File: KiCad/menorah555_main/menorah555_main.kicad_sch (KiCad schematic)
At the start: 100 parts, among them J1 USB_B_Micro, J2 Jack5.5x2.1, J3 Plug5.5x2.1, Q1 MMBT3904, Q10 MJD31, Q2 MMBT3904, Q3 MMBT3904, Q4 MMBT3904, Q5 MMBT3904, Q6 MMBT3904, Q7 MMBT3904, Q8 MMBT3904, Q9 MMBT3904, SW1 SW_Reed, SW2 SW_Reed, SW3 SW_Reed, SW4 SW_Reed, SW5 SW_Reed, SW6 SW_Reed, SW7 SW_Reed, SW8 SW_Reed, SW9 SW_DPDT, U1 TLC555, U2 TLC555, U3 TLC555, U4 TLC555, U5 TLC555, U6 TLC555, U7 TLC555, U8 TLC555, U9 TLC555

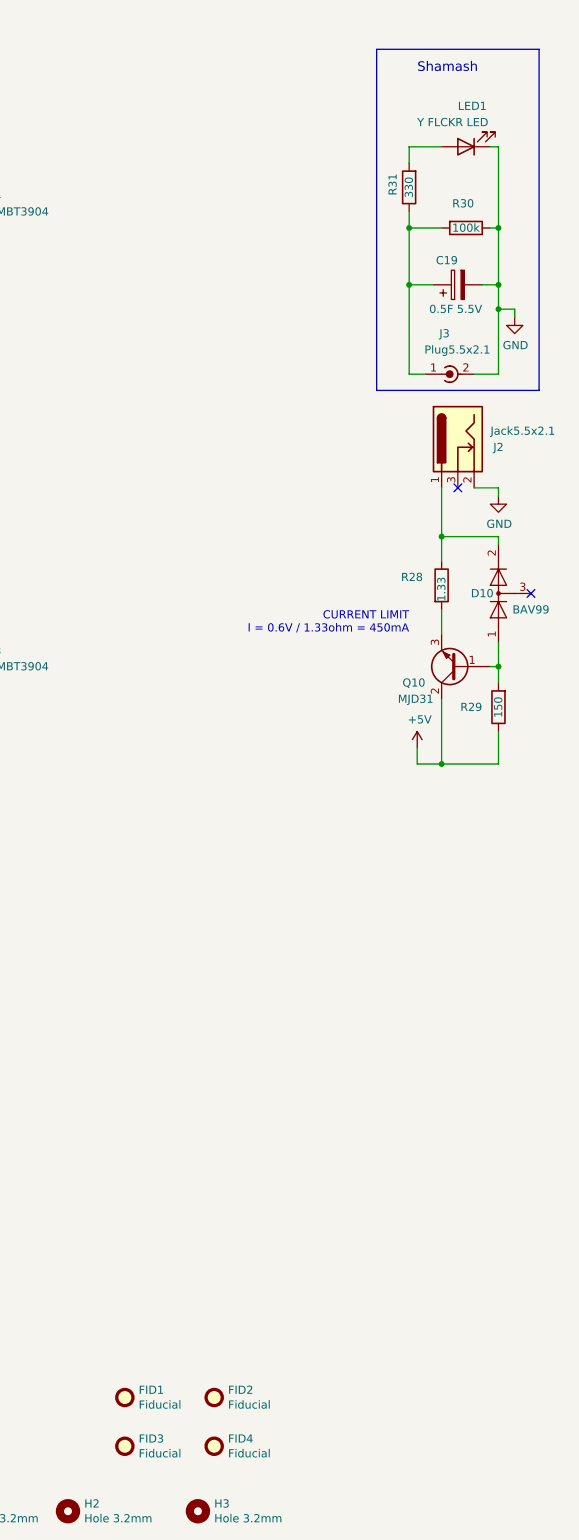
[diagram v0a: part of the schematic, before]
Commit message: Split PCB into separate main and shamash boards
Previously, the main and shamash PCBs were combined into one file.
Now they are separate PCBs so that they don't need to be cut apart and
smoothed.
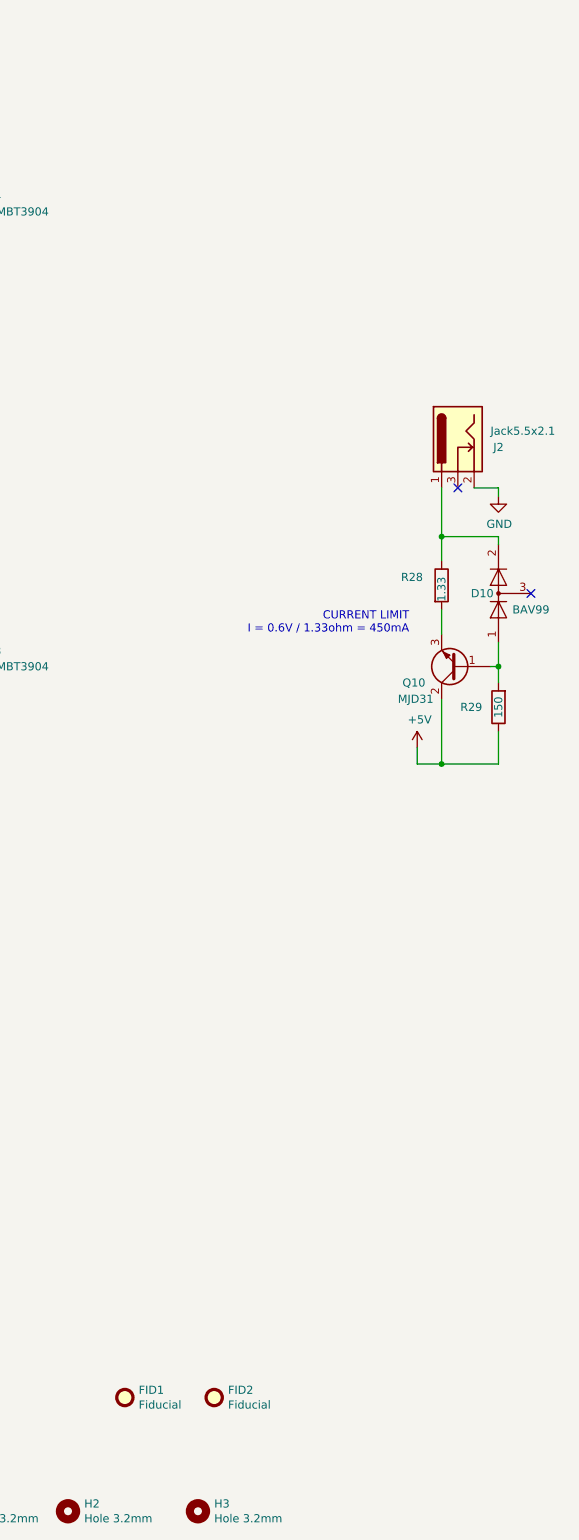
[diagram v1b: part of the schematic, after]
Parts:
- removed C19: 0.5F 5.5V, 0_my_footprints:CP_Supercap_DGH504Q5R5_Horizontal, symbol Device:CP
- removed FID3, FID4: Fiducial, Fiducial:Fiducial_1mm_Mask2mm, symbol Mechanical:Fiducial
- removed J3: Plug5.5x2.1, 0_my_footprints:KobiConn_173-5521TIP-EX_power_plug, symbol Connector:Conn_Coaxial_Power
- removed LED1: Y FLCKR LED, 0_my_footprints:LED_D5.0mm_Horizontal_SMT_O3.81mm_Z3.0mm, symbol Device:LED
- removed R30: 100k, Resistor_SMD:R_0805_2012Metric, symbol Device:R
- removed R31: 330, Resistor_SMD:R_0805_2012Metric, symbol Device:R
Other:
- note removed: "Shamash"
- title: Menorah555 -> Menorah555 Main

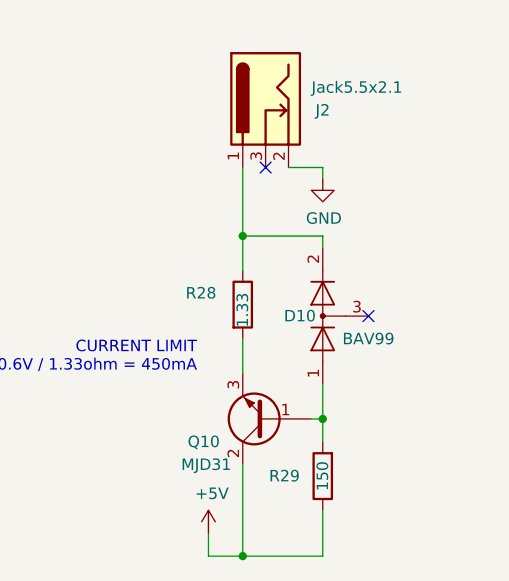
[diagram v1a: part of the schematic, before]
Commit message: Fixed long turn-off time
Previously on the rev A PCB (PCB2002A), when power was turned off, the
shamash would take a very long time (> 20 minutes) to fully turn off.
Now a new diode, D11, has been added to drain the supercap when power is
turned off with the switch.
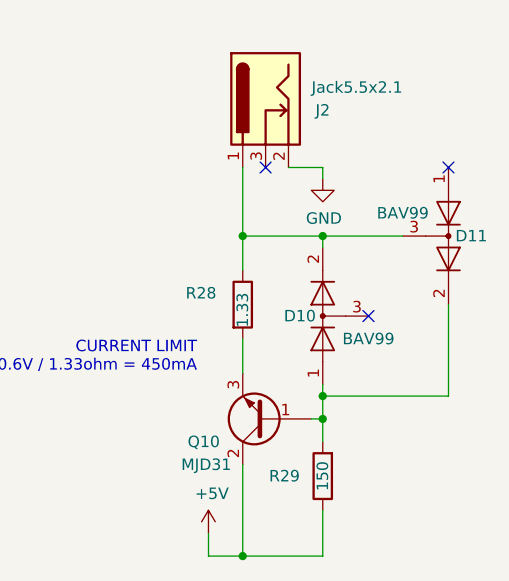
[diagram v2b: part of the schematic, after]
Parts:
- added D11: BAV99, Package_TO_SOT_SMD:SOT-23, symbol Diode:BAV99
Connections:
- net at D10.2 (A), J2.1, R28.1: now also D11.3 (K)
- net at D10.1 (K), Q10.1 (B), R29.2: now also D11.2 (A)
- no-connect marks 15 -> 16
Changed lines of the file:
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@@
   (junction (at 154.94 184.15) (diameter 0) (color 0 0 0 0)
   )
+  (junction (at 342.9 107.95) (diameter 0) (color 0 0 0 0)
+  )
   (junction (at 82.55 207.01) (diameter 0) (color 0 0 0 0)
   )
+  (junction (at 342.9 125.73) (diameter 0) (color 0 0 0 0)
+  )
   (junction (at 191.77 119.38) (diameter 0) (color 0 0 0 0)
   )
@@
   (no_connect (at 135.89 69.85))
   (no_connect (at 190.5 140.97))
+  (no_connect (at 356.87 100.33))
   (no_connect (at 246.38 140.97))
   (wire (pts (xy 110.49 135.89) (xy 109.22 135.89))
@@
     (stroke (width 0) (type default) (color 0 0 0 0))
   )
+  (wire (pts (xy 356.87 125.73) (xy 342.9 125.73))
+    (stroke (width 0) (type default) (color 0 0 0 0))
+  )
   (wire (pts (xy 93.98 31.75) (xy 92.71 31.75))
     (stroke (width 0) (type default) (color 0 0 0 0))
@@
     (stroke (width 0) (type default) (color 0 0 0 0))
   )
+  (wire (pts (xy 356.87 115.57) (xy 356.87 125.73))
+    (stroke (width 0) (type default) (color 0 0 0 0))
+  )
   (wire (pts (xy 241.3 110.49) (xy 241.3 119.38))
     (stroke (width 0) (type default) (color 0 0 0 0))
@@
     (stroke (width 0) (type default) (color 0 0 0 0))
   )
+  (wire (pts (xy 342.9 125.73) (xy 342.9 128.27))
+    (stroke (width 0) (type default) (color 0 0 0 0))
+  )
   (wire (pts (xy 219.71 48.26) (xy 241.3 48.26))
     (stroke (width 0) (type default) (color 0 0 0 0))
@@
     (stroke (width 0) (type default) (color 0 0 0 0))
   )
+  (wire (pts (xy 342.9 107.95) (xy 351.79 107.95))
+    (stroke (width 0) (type default) (color 0 0 0 0))
+  )
   (wire (pts (xy 81.28 119.38) (xy 93.98 119.38))
     (stroke (width 0) (type default) (color 0 0 0 0))
@@
     (stroke (width 0) (type default) (color 0 0 0 0))
   )
-  (wire (pts (xy 342.9 124.46) (xy 342.9 128.27))
+  (wire (pts (xy 342.9 124.46) (xy 342.9 125.73))
     (stroke (width 0) (type default) (color 0 0 0 0))
   )
@@
     (pin "1")
   )
+  (symbol (lib_id "Diode:BAV99") (at 356.87 107.95 270) (unit 1)
+    (in_bom yes) (on_board yes)
+    (property "Reference" "D11" (id 0) (at 359.41 107.95 90))
+    (property "Value" "BAV99" (id 1) (at 351.79 105.41 90))
+    (property "Footprint" "Package_TO_SOT_SMD:SOT-23" (id 2) (at 344.17 107.95 0)
+      (effects (font (size 1.27 1.27)) hide)
+    )
+    (property "Datasheet" "https://assets.nexperia.com/documents/data-sheet/BAV99_SER.pdf" (id 3) (at 356.87 107.95 0)
+      (effects (font (size 1.27 1.27)) hide)
+    )
+    (property "Source" "Mouser 241-BAV99_R1_00001" (id 4) (at 356.87 107.95 0)
+      (effects (font (size 1.27 1.27)) hide)
+    )
+    (pin "1")
+    (pin "2")
+    (pin "3")
+  )
   (sheet_instances
     (path "/" (page "1"))
@@
       (reference "D10") (unit 1) (value "BAV99") (footprint "Package_TO_SOT_SMD:SOT-23")
     )
+    (path "/a73e6f72-062a-4c4e-9d81-60bd2ec9e556"
+      (reference "D11") (unit 1) (value "BAV99") (footprint "Package_TO_SOT_SMD:SOT-23")
+    )
     (path "/00000000-0000-0000-0000-0000607f6d29"

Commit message: Made USB footprint hand-solderable
The USB footprint was changed to be an Amphenol 10118194-0001LF so that
it could be hand-soldered if desired.
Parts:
- J1: footprint 0_my_footprints:MOLEX_47590-0001 -> 0_my_footprints:AMPHENOL_10118194-0001LF; symbol Connector:USB_B_Micro -> 0_project_symbol_library:Amphenol_10118194-0001LF_USB_B_Micro
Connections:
- net GND: now also J1.S1 (Shield), J1.S2 (Shield), J1.S3 (Shield), J1.S4 (Shield), J1.S5 (Shield), J1.S6 (Shield)
- removed net SHLD: J1.6 (Shield)
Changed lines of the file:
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@@
     (stroke (width 0) (type default) (color 0 0 0 0))
   )
-  (wire (pts (xy 52.07 222.25) (xy 60.96 222.25))
-    (stroke (width 0) (type default) (color 0 0 0 0))
-  )
   (wire (pts (xy 85.09 212.09) (xy 83.82 212.09))
     (stroke (width 0) (type default) (color 0 0 0 0))
@@
     (stroke (width 0) (type default) (color 0 0 0 0))
   )
+  (wire (pts (xy 60.96 223.52) (xy 58.42 223.52))
+    (stroke (width 0) (type default) (color 0 0 0 0))
+  )
   (wire (pts (xy 220.98 135.89) (xy 219.71 135.89))
     (stroke (width 0) (type default) (color 0 0 0 0))
@@
     (stroke (width 0) (type default) (color 0 0 0 0))
   )
+  (wire (pts (xy 60.96 222.25) (xy 60.96 223.52))
+    (stroke (width 0) (type default) (color 0 0 0 0))
+  )
   (wire (pts (xy 260.35 50.8) (xy 260.35 48.26))
     (stroke (width 0) (type default) (color 0 0 0 0))
@@
     (effects (font (size 1.27 1.27)) (justify left bottom))
   )
-  (label "SHLD" (at 53.34 222.25 0)
-    (effects (font (size 1.27 1.27)) (justify left bottom))
-  )
   (label "RST_N" (at 156.21 146.05 0)
     (effects (font (size 1.27 1.27)) (justify left bottom))
@@
     (pin "6")
   )
-  (symbol (lib_id "Connector:USB_B_Micro") (at 63.5 212.09 0) (unit 1)
+  (symbol (lib_id "0_project_symbol_library:Amphenol_10118194-0001LF_USB_B_Micro") (at 63.5 212.09 0) (unit 1)
     (in_bom yes) (on_board yes)
     (property "Reference" "J1" (id 0) (at 64.9478 200.2282 0))
     (property "Value" "USB_B_Micro" (id 1) (at 64.9478 202.5396 0))
-    (property "Footprint" "0_my_footprints:MOLEX_47590-0001" (id 2) (at 67.31 213.36 0)
+    (property "Footprint" "0_my_footprints:AMPHENOL_10118194-0001LF" (id 2) (at 67.31 213.36 0)
       (effects (font (size 1.27 1.27)) hide)
     )
@@
     (pin "4")
     (pin "5")
-    (pin "6")
+    (pin "S1")
+    (pin "S2")
+    (pin "S3")
+    (pin "S4")
+    (pin "S5")
+    (pin "S6")
   )
   (symbol (lib_id "power:GND") (at 63.5 223.52 0) (unit 1)
@@
     (pin "1")
   )
+  (symbol (lib_id "power:GND") (at 58.42 223.52 0) (unit 1)
+    (in_bom yes) (on_board yes)
+    (property "Reference" "#PWR?" (id 0) (at 58.42 229.87 0)
+      (effects (font (size 1.27 1.27)) hide)
+    )
+    (property "Value" "GND" (id 1) (at 58.547 227.9142 0))
+    (property "Footprint" "" (id 2) (at 58.42 223.52 0)
+      (effects (font (size 1.27 1.27)) hide)
+    )
+    (property "Datasheet" "" (id 3) (at 58.42 223.52 0)
+      (effects (font (size 1.27 1.27)) hide)
+    )
+    (pin "1")
+  )
   (symbol (lib_id "Diode:BAV99") (at 356.87 107.95 270) (unit 1)
     (in_bom yes) (on_board yes)
@@
       (reference "#PWR0102") (unit 1) (value "+5V") (footprint "")
     )
+    (path "/237754d7-4fd7-465f-a843-defefeb151d7"
+      (reference "#PWR?") (unit 1) (value "GND") (footprint "")
+    )
     (path "/00000000-0000-0000-0000-000061aca084"
       (reference "C1") (unit 1) (value "10nF") (footprint "Capacitor_SMD:C_0805_2012Metric")
@@
     )
     (path "/00000000-0000-0000-0000-000061bafea9"
-      (reference "J1") (unit 1) (value "USB_B_Micro") (footprint "0_my_footprints:MOLEX_47590-0001")
+      (reference "J1") (unit 1) (value "USB_B_Micro") (footprint "0_my_footprints:AMPHENOL_10118194-0001LF")
     )
     (path "/00000000-0000-0000-0000-000061c09a96"

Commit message: Eliminated silkscreen crossing edge cuts
The DRC was giving warnings for silkscreen that overlapped with edge
cuts because it was getting cut by the soldermask. The footprints for
the LEDs and the shamash power connector were updated to delete the
silkscreen outside of the board edge cuts
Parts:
- LED2, LED3, LED4, LED5, LED6, LED7, LED8, LED9: footprint 0_my_footprints:LED_D5.0mm_Horizontal_SMT_O3.81mm_Z3.0mm -> 0_menorah555:LED_D5.0mm_Horizontal_SMT_O3.81mm
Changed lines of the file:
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@@
       (effects (font (size 1.27 1.27)) (justify right))
     )
-    (property "Footprint" "0_my_footprints:LED_D5.0mm_Horizontal_SMT_O3.81mm_Z3.0mm" (id 2) (at 88.9 31.75 0)
+    (property "Footprint" "0_menorah555:LED_D5.0mm_Horizontal_SMT_O3.81mm" (id 2) (at 88.9 31.75 0)
       (effects (font (size 1.27 1.27)) hide)
     )
@@
       (effects (font (size 1.27 1.27)) (justify right))
     )
-    (property "Footprint" "0_my_footprints:LED_D5.0mm_Horizontal_SMT_O3.81mm_Z3.0mm" (id 2) (at 144.78 31.75 0)
+    (property "Footprint" "0_menorah555:LED_D5.0mm_Horizontal_SMT_O3.81mm" (id 2) (at 144.78 31.75 0)
       (effects (font (size 1.27 1.27)) hide)
     )
@@
       (effects (font (size 1.27 1.27)) (justify right))
     )
-    (property "Footprint" "0_my_footprints:LED_D5.0mm_Horizontal_SMT_O3.81mm_Z3.0mm" (id 2) (at 199.39 31.75 0)
+    (property "Footprint" "0_menorah555:LED_D5.0mm_Horizontal_SMT_O3.81mm" (id 2) (at 199.39 31.75 0)
       (effects (font (size 1.27 1.27)) hide)
     )
@@
       (effects (font (size 1.27 1.27)) (justify right))
     )
-    (property "Footprint" "0_my_footprints:LED_D5.0mm_Horizontal_SMT_O3.81mm_Z3.0mm" (id 2) (at 255.27 31.75 0)
+    (property "Footprint" "0_menorah555:LED_D5.0mm_Horizontal_SMT_O3.81mm" (id 2) (at 255.27 31.75 0)
       (effects (font (size 1.27 1.27)) hide)
     )
@@
       (effects (font (size 1.27 1.27)) (justify right))
     )
-    (property "Footprint" "0_my_footprints:LED_D5.0mm_Horizontal_SMT_O3.81mm_Z3.0mm" (id 2) (at 88.9 102.87 0)
+    (property "Footprint" "0_menorah555:LED_D5.0mm_Horizontal_SMT_O3.81mm" (id 2) (at 88.9 102.87 0)
       (effects (font (size 1.27 1.27)) hide)
     )
@@
       (effects (font (size 1.27 1.27)) (justify right))
     )
-    (property "Footprint" "0_my_footprints:LED_D5.0mm_Horizontal_SMT_O3.81mm_Z3.0mm" (id 2) (at 144.78 102.87 0)
+    (property "Footprint" "0_menorah555:LED_D5.0mm_Horizontal_SMT_O3.81mm" (id 2) (at 144.78 102.87 0)
       (effects (font (size 1.27 1.27)) hide)
     )
@@
       (effects (font (size 1.27 1.27)) (justify right))
     )
-    (property "Footprint" "0_my_footprints:LED_D5.0mm_Horizontal_SMT_O3.81mm_Z3.0mm" (id 2) (at 199.39 102.87 0)
+    (property "Footprint" "0_menorah555:LED_D5.0mm_Horizontal_SMT_O3.81mm" (id 2) (at 199.39 102.87 0)
       (effects (font (size 1.27 1.27)) hide)
     )
@@
       (effects (font (size 1.27 1.27)) (justify right))
     )
-    (property "Footprint" "0_my_footprints:LED_D5.0mm_Horizontal_SMT_O3.81mm_Z3.0mm" (id 2) (at 255.27 102.87 0)
+    (property "Footprint" "0_menorah555:LED_D5.0mm_Horizontal_SMT_O3.81mm" (id 2) (at 255.27 102.87 0)
       (effects (font (size 1.27 1.27)) hide)
     )
@@
   (symbol (lib_id "power:GND") (at 58.42 223.52 0) (unit 1)
     (in_bom yes) (on_board yes)
-    (property "Reference" "#PWR?" (id 0) (at 58.42 229.87 0)
+    (property "Reference" "#PWR0101" (id 0) (at 58.42 229.87 0)
       (effects (font (size 1.27 1.27)) hide)
     )
@@
       (reference "#PWR075") (unit 1) (value "GND") (footprint "")
     )
+    (path "/237754d7-4fd7-465f-a843-defefeb151d7"
+      (reference "#PWR0101") (unit 1) (value "GND") (footprint "")
+    )
     (path "/00000000-0000-0000-0000-00006218b3a7"
       (reference "#PWR0102") (unit 1) (value "+5V") (footprint "")
     )
-    (path "/237754d7-4fd7-465f-a843-defefeb151d7"
-      (reference "#PWR?") (unit 1) (value "GND") (footprint "")
-    )
     (path "/00000000-0000-0000-0000-000061aca084"
       (reference "C1") (unit 1) (value "10nF") (footprint "Capacitor_SMD:C_0805_2012Metric")
@@
     )
     (path "/00000000-0000-0000-0000-000061ad1d8d"
-      (reference "LED2") (unit 1) (value "Y FLCKR LED") (footprint "0_my_footprints:LED_D5.0mm_Horizontal_SMT_O3.81mm_Z3.0mm")
+      (reference "LED2") (unit 1) (value "Y FLCKR LED") (footprint "0_menorah555:LED_D5.0mm_Horizontal_SMT_O3.81mm")
     )
     (path "/00000000-0000-0000-0000-000061d46191"
-      (reference "LED3") (unit 1) (value "Y FLCKR LED") (footprint "0_my_footprints:LED_D5.0mm_Horizontal_SMT_O3.81mm_Z3.0mm")
+      (reference "LED3") (unit 1) (value "Y FLCKR LED") (footprint "0_menorah555:LED_D5.0mm_Horizontal_SMT_O3.81mm")
     )
     (path "/00000000-0000-0000-0000-000061d58194"
-      (reference "LED4") (unit 1) (value "Y FLCKR LED") (footprint "0_my_footprints:LED_D5.0mm_Horizontal_SMT_O3.81mm_Z3.0mm")
+      (reference "LED4") (unit 1) (value "Y FLCKR LED") (footprint "0_menorah555:LED_D5.0mm_Horizontal_SMT_O3.81mm")
     )
     (path "/00000000-0000-0000-0000-000061d58224"
-      (reference "LED5") (unit 1) (value "Y FLCKR LED") (footprint "0_my_footprints:LED_D5.0mm_Horizontal_SMT_O3.81mm_Z3.0mm")
+      (reference "LED5") (unit 1) (value "Y FLCKR LED") (footprint "0_menorah555:LED_D5.0mm_Horizontal_SMT_O3.81mm")
     )
     (path "/00000000-0000-0000-0000-000061e9d611"
-      (reference "LED6") (unit 1) (value "Y FLCKR LED") (footprint "0_my_footprints:LED_D5.0mm_Horizontal_SMT_O3.81mm_Z3.0mm")
+      (reference "LED6") (unit 1) (value "Y FLCKR LED") (footprint "0_menorah555:LED_D5.0mm_Horizontal_SMT_O3.81mm")
     )
     (path "/00000000-0000-0000-0000-000061e9d6a1"
-      (reference "LED7") (unit 1) (value "Y FLCKR LED") (footprint "0_my_footprints:LED_D5.0mm_Horizontal_SMT_O3.81mm_Z3.0mm")
+      (reference "LED7") (unit 1) (value "Y FLCKR LED") (footprint "0_menorah555:LED_D5.0mm_Horizontal_SMT_O3.81mm")
     )
     (path "/00000000-0000-0000-0000-000061e9d731"
-      (reference "LED8") (unit 1) (value "Y FLCKR LED") (footprint "0_my_footprints:LED_D5.0mm_Horizontal_SMT_O3.81mm_Z3.0mm")
+      (reference "LED8") (unit 1) (value "Y FLCKR LED") (footprint "0_menorah555:LED_D5.0mm_Horizontal_SMT_O3.81mm")
     )
     (path "/00000000-0000-0000-0000-000061e9d7c1"
-      (reference "LED9") (unit 1) (value "Y FLCKR LED") (footprint "0_my_footprints:LED_D5.0mm_Horizontal_SMT_O3.81mm_Z3.0mm")
+      (reference "LED9") (unit 1) (value "Y FLCKR LED") (footprint "0_menorah555:LED_D5.0mm_Horizontal_SMT_O3.81mm")
     )
     (path "/00000000-0000-0000-0000-000060735e73"

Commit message: Offset the J2 model in Z direction
The 3d model for the J2 power jack has been offset by 2.35mm so that it
will make the main PCB and shamash PCB line up.
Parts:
- J2: footprint 0_my_footprints:Gravitech_CONSOCJ2155_2.1mm_5.5mm_Barrel_Jack -> 0_menorah555:Gravitech_CONSOCJ2155_2.1mm_5.5mm_Barrel_Jack_Z2.35
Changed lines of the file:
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@@
     (property "Reference" "J2" (id 0) (at 342.9 93.98 90))
     (property "Value" "Jack5.5x2.1" (id 1) (at 346.71 91.44 90))
-    (property "Footprint" "0_my_footprints:Gravitech_CONSOCJ2155_2.1mm_5.5mm_Barrel_Jack" (id 2) (at 337.566 93.98 0)
+    (property "Footprint" "0_menorah555:Gravitech_CONSOCJ2155_2.1mm_5.5mm_Barrel_Jack_Z2.35" (id 2) (at 337.566 93.98 0)
       (effects (font (size 1.27 1.27)) hide)
     )
@@
     )
     (path "/00000000-0000-0000-0000-000061c09a96"
-      (reference "J2") (unit 1) (value "Jack5.5x2.1") (footprint "0_my_footprints:Gravitech_CONSOCJ2155_2.1mm_5.5mm_Barrel_Jack")
+      (reference "J2") (unit 1) (value "Jack5.5x2.1") (footprint "0_menorah555:Gravitech_CONSOCJ2155_2.1mm_5.5mm_Barrel_Jack_Z2.35")
     )
     (path "/00000000-0000-0000-0000-000061ad1d8d"
